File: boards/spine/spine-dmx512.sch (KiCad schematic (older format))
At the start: 22 parts, among them CON6 XLR-3 Female, Q1 IRFML8244, Q2 IRFML8244, T1 10/100baseT transformer, U3 NC7WZ14, U5 NC7WZ14, U6 SN75176B

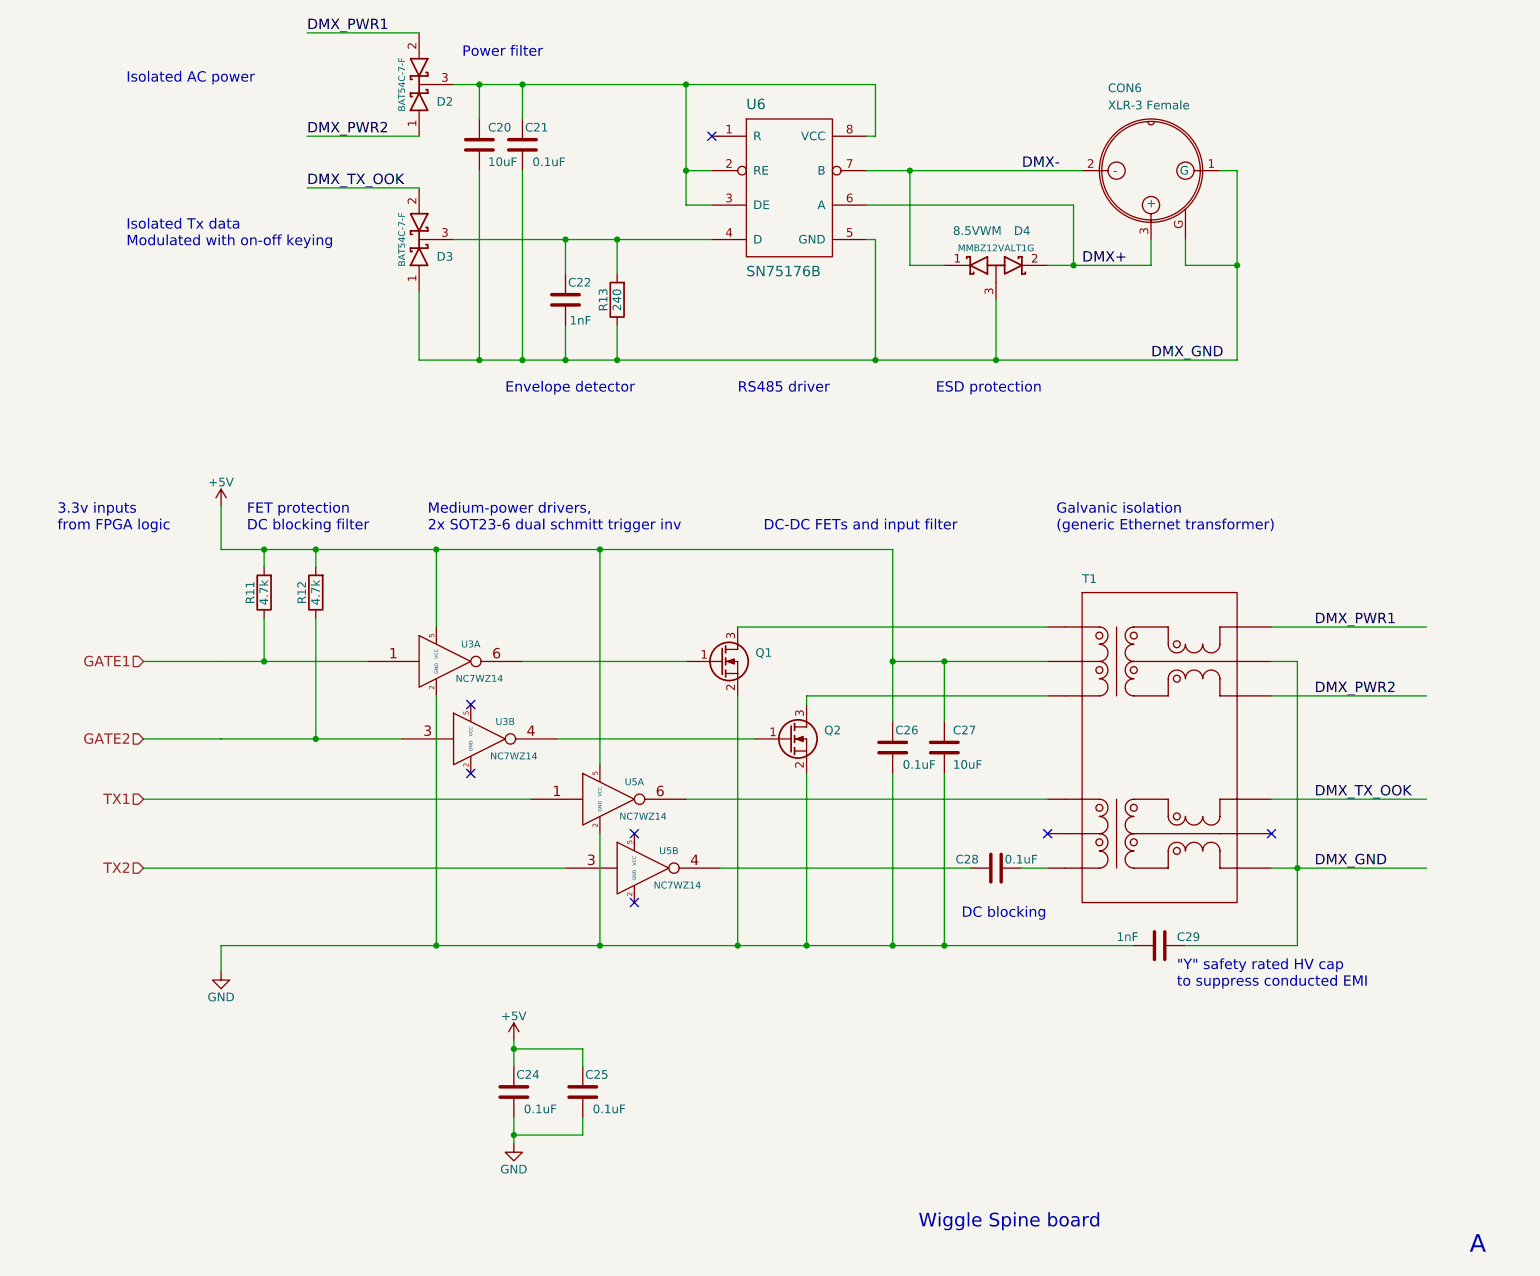
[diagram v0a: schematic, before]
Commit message: Redraw DMX isolator based on latest simplifications
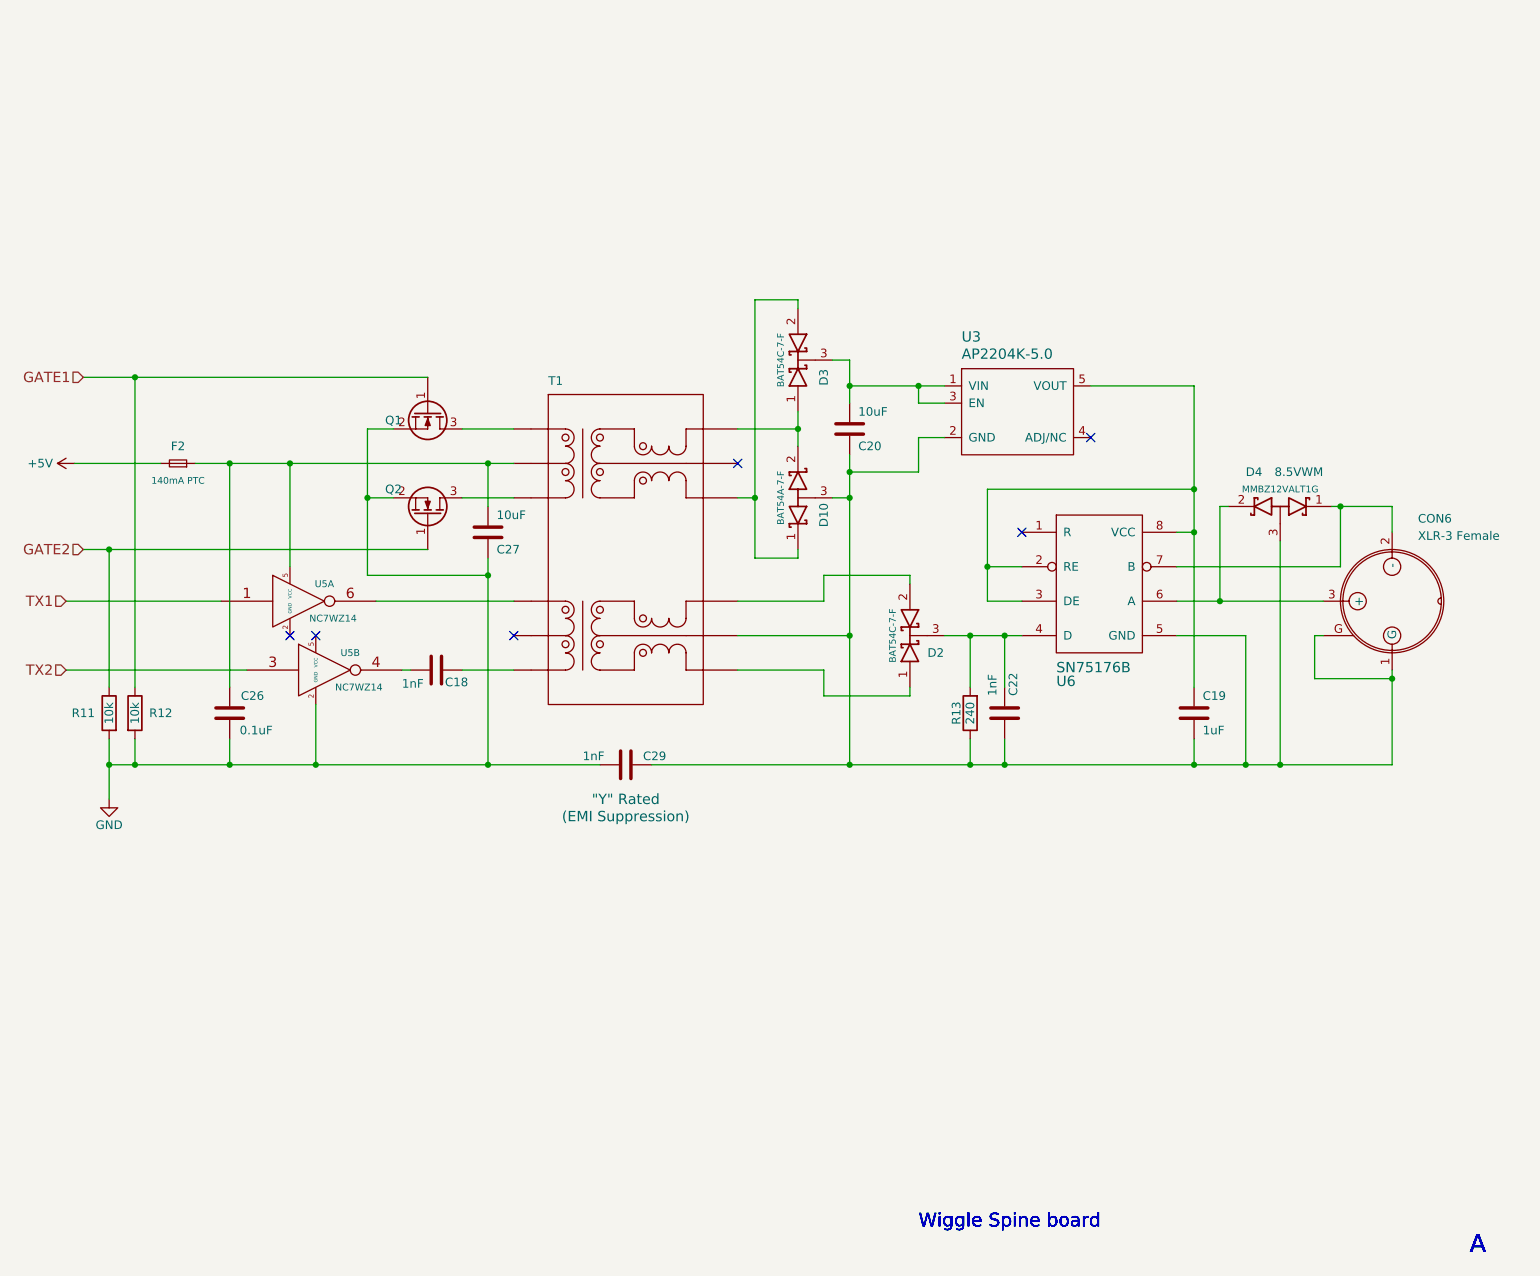
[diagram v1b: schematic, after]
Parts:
- removed C21, C24, C25, C28: 0.1uF, Capacitors_SMD:C_0805, symbol C
- removed U3: NC7WZ14, TO_SOT_Packages_SMD:SC-70-6, symbol NC7WZ14
- added C18: 1nF, Capacitors_SMD:C_0805, symbol C
- added C19: 1uF, Capacitors_SMD:C_0805, symbol C
- added D10: BAT54 2x common anode, TO_SOT_Packages_SMD:SOT-23, symbol D_Schottky_x2_ACom_KKA
- added F2: 140mA PTC, Resistors_SMD:R_1812, symbol F_Small
- added U3: AP2204K-5.0, TO_SOT_Packages_SMD:SOT-23-5, symbol AP2204
- C20: value 10uF -> 10uF
- C29: Description (none) -> (EMI Suppression); Safety Rating (none) -> \"Y\" Rated
- R11, R12: value 4.7k -> 10k; MfgId RMCF0805JT4K70 -> RMCF0805JT10K0; Vend1Id RMCF0805JT4K70CT-ND -> RMCF0805JT10K0CT-ND
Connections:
- net labels removed: DMX+, DMX-, DMX_GND, DMX_PWR1, DMX_PWR2, DMX_TX_OOK
- wire segments 113 -> 114
- no-connect marks 7 -> 6
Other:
- note removed: ""Y" safety rated HV cap\nto suppress conducted EMI"
- note removed: "3.3v inputs\nfrom FPGA logic"
- note removed: "DC blocking"
- note removed: "DC-DC FETs and input filter"
- note removed: "ESD protection"
- note removed: "Envelope detector"
- note removed: "FET protection\nDC blocking filter"
- note removed: "Galvanic isolation\n(generic Ethernet transformer)"
- note removed: "Isolated AC power"
- note removed: "Isolated Tx data\nModulated with on-off keying"
- note removed: "Medium-power drivers,\n2x SOT23-6 dual schmitt trigger inv"
- note removed: "Power filter"
- note removed: "RS485 driver"
- moved on the sheet: C20, C22, C26, C27, C29, CON6, D2, D3, D4, Q2, R13, T1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

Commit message: More simplification and BOM optimization
Thanks for the hints on the ST485 and dual-FETs, @mikelectricstuf!
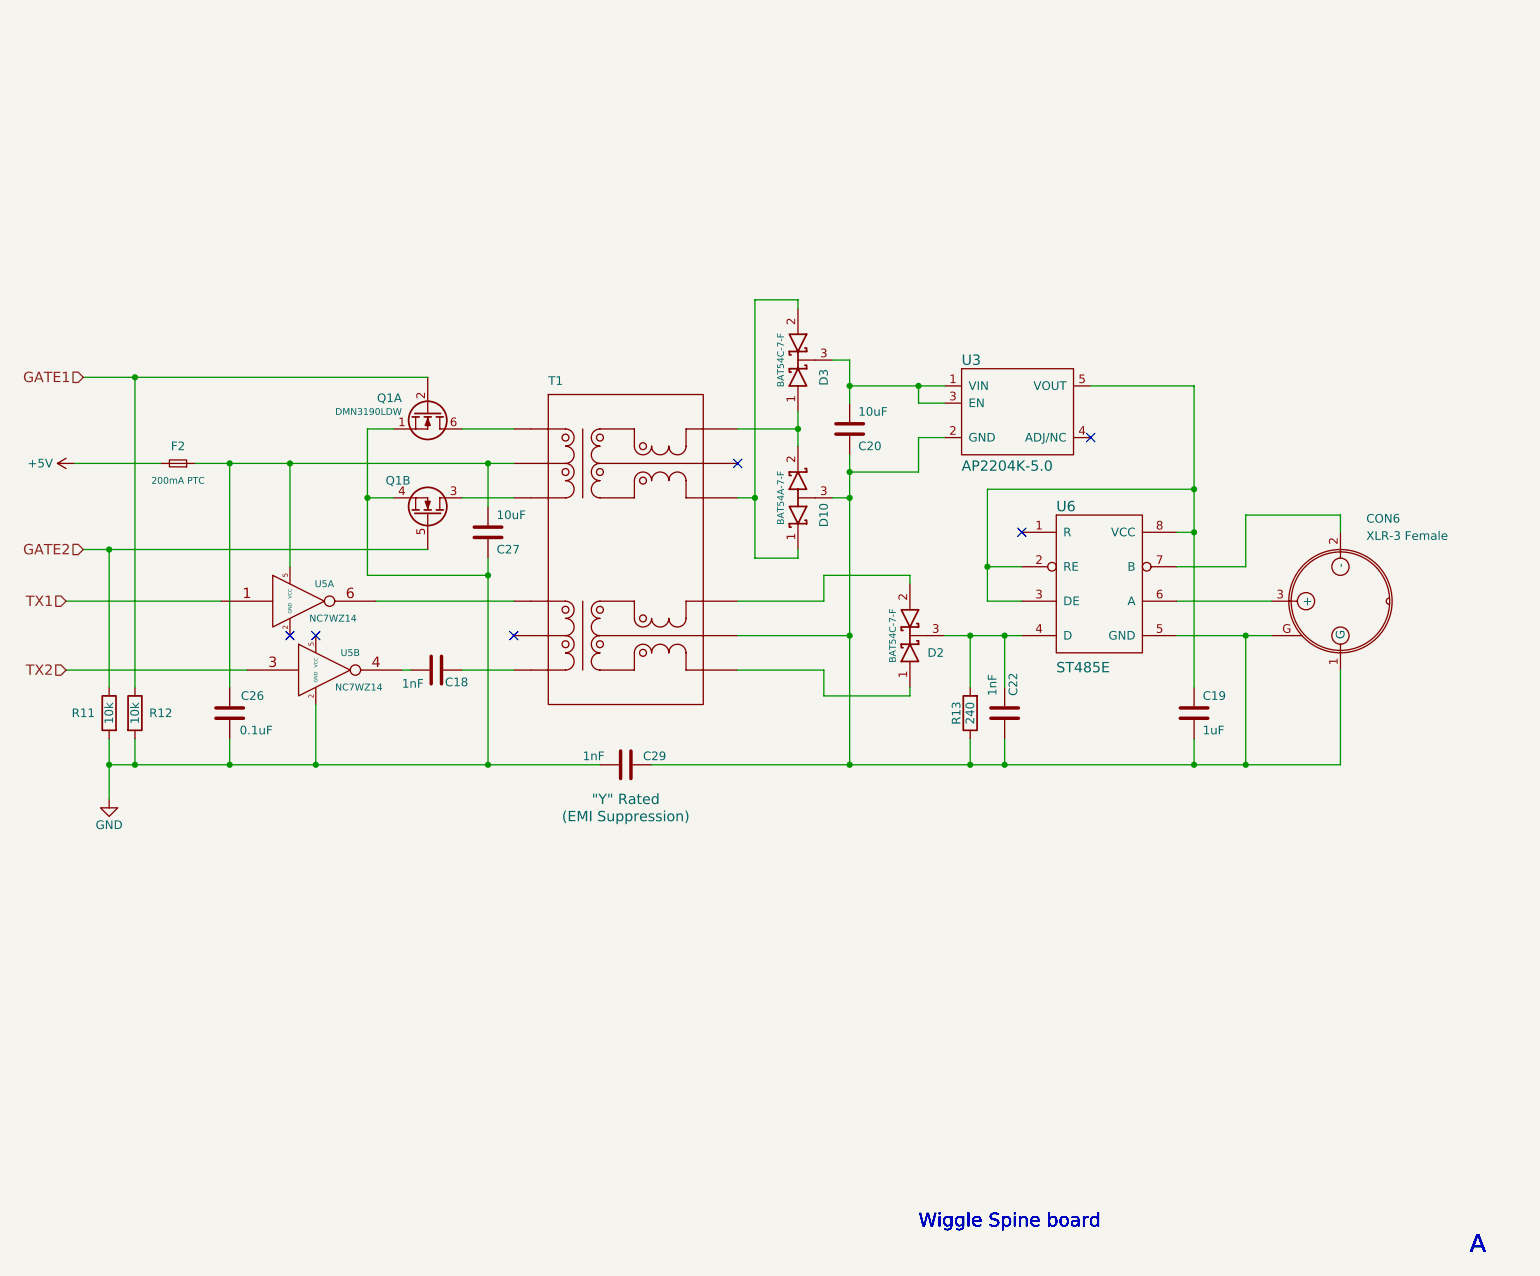
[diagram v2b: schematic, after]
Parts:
- removed D4: 8.5VWM, TO_SOT_Packages_SMD:SOT-23, symbol D_Schottky_x2_ACom_KKA
- removed Q1, Q2: IRFML8244, TO_SOT_Packages_SMD:SOT-23, symbol Q_NMOS_GSD
- added Q1: DMN3190LDW, TO_SOT_Packages_SMD:SC-70-6, symbol Q_NMOS_SGDSGD
- C29: MfgId EPCOS (TDK) -> B32021A3102M189; MfrId B32021A3102M189 -> EPCOS (TDK)
- F2: value 140mA PTC -> 200mA PTC; footprint Resistors_SMD:R_1812 -> Resistors_SMD:R_1206; MfgId 0ZCG0014FF2C -> 0ZCJ0020FF2E; Vend1Id 507-1755-1-ND -> 507-1797-1-ND
- U6: value SN75176B -> ST485E; MfgId SN75176BDR -> ST485ECDR; MfrId Texas Instruments -> STMicroelectronics; RefPrice1k 0.330 -> 0.40145; Vend1Id 296-1275-1-ND -> 497-3735-1-ND
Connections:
- net GATE1: now also Q1.2 (G)
- net GATE2: now also Q1.5 (G)
- net GND: now also Q1.1 (S), Q1.4 (S)
- net at T1.14: now also Q1.3 (D)
- net at T1.16: now also Q1.6 (D)
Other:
- moved on the sheet: CON6
